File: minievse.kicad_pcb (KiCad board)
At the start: 2 copper layers, 76.2 x 50.8 mm, 27 parts, among them IC1 ATMEGA328P-P, P1 SERIAL, P2 -- 12V ++, P3 ICSP, P4 Pilot, P5 RELAYCOIL, SW1 RESET, U1 7805, U2 IXDD604PI, X1 16MHz

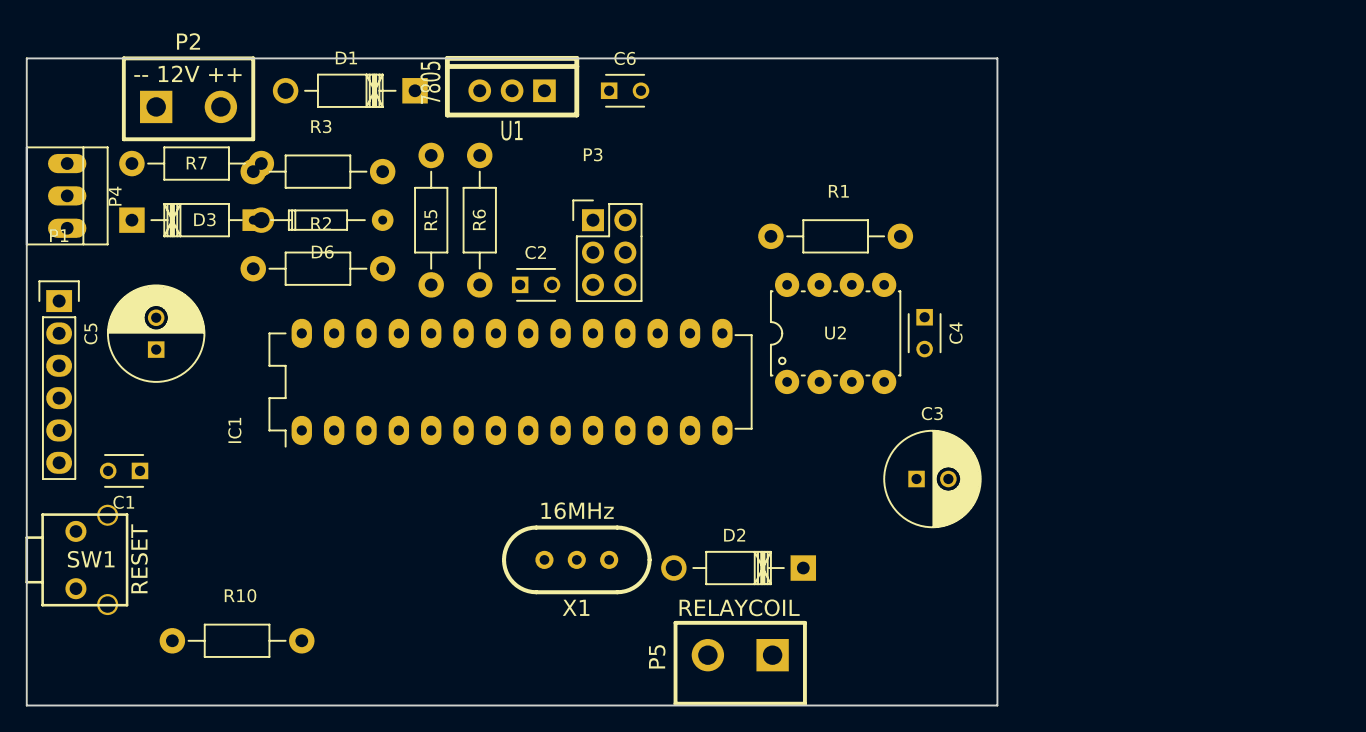
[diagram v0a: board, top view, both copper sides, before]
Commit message: placed parts on the board, ready for traces
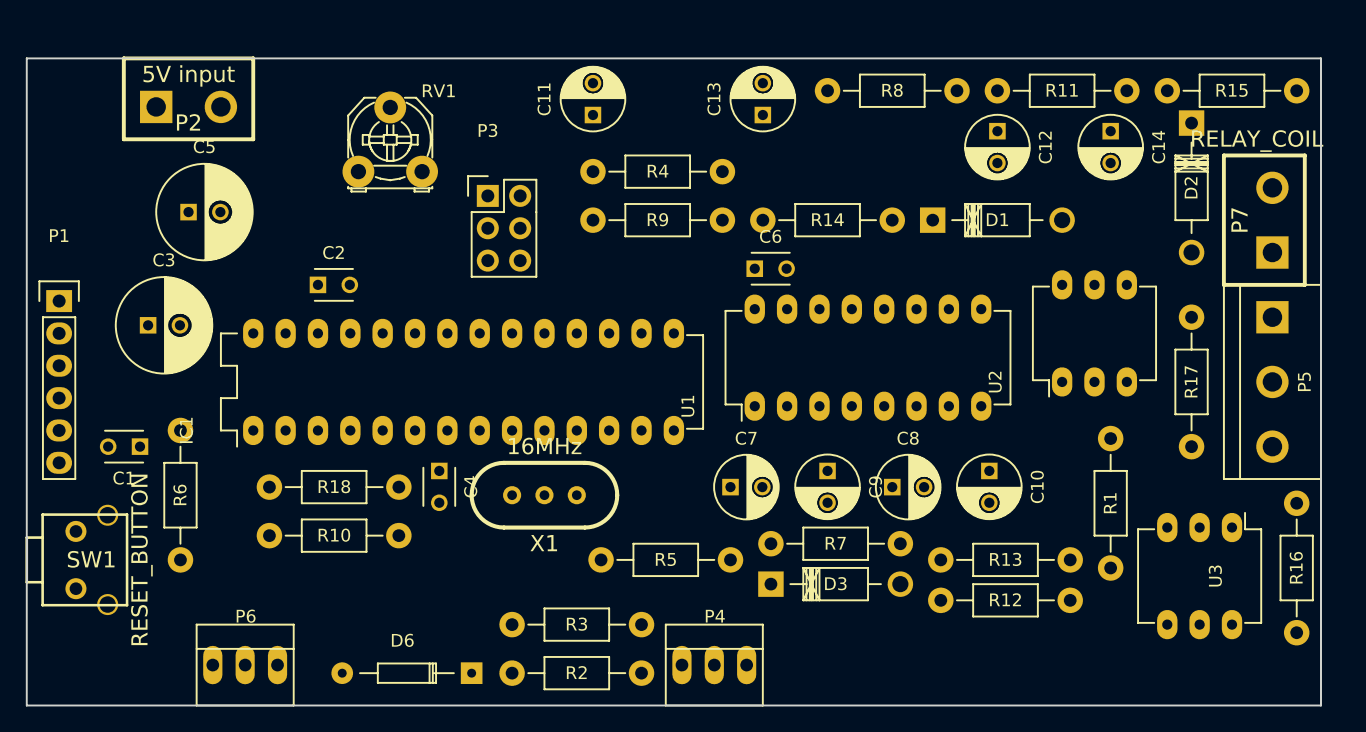
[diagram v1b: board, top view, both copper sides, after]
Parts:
- added C10: 1uF, Capacitors_ThroughHole:C_Radial_D5_L6_P2.5, F.Cu at (101.0, 57.8)
- added C11: 10uF, Capacitors_ThroughHole:C_Radial_D5_L6_P2.5, F.Cu at (69.8, 29.8)
- added C12: 10uF, Capacitors_ThroughHole:C_Radial_D5_L6_P2.5, F.Cu at (101.6, 31.1)
- added C13: 10uF, Capacitors_ThroughHole:C_Radial_D5_L6_P2.5, F.Cu at (83.2, 29.8)
- added C14: 10uF, Capacitors_ThroughHole:C_Radial_D5_L6_P2.5, F.Cu at (110.5, 31.1)
- added C7: 1uF, Capacitors_ThroughHole:C_Radial_D5_L6_P2.5, F.Cu at (80.6, 59.1)
- added C8: 1uF, Capacitors_ThroughHole:C_Radial_D5_L6_P2.5, F.Cu at (93.3, 59.1)
- added C9: 1uF, Capacitors_ThroughHole:C_Radial_D5_L6_P2.5, F.Cu at (88.3, 57.8)
- added P6: LED_STRIP, Connect:PINHEAD1-3, F.Cu at (42.5, 73.0)
- added P7: RELAY_COIL, battery-dlg:CCFLHV, F.Cu at (123.2, 38.1)
- added R11: 2550, wishparts:Resistor_Horizontal_RM10mm_refdes_in_box, F.Cu at (111.8, 27.9)
- added R12: 1200, wishparts:Resistor_Horizontal_RM10mm_refdes_in_box, F.Cu at (97.2, 67.9)
- added R13: 1200, wishparts:Resistor_Horizontal_RM10mm_refdes_in_box, F.Cu at (97.2, 64.8)
- added R14: 50K, wishparts:Resistor_Horizontal_RM10mm_refdes_in_box, F.Cu at (83.2, 38.1)
- added R15: 50K, wishparts:Resistor_Horizontal_RM10mm_refdes_in_box, F.Cu at (114.9, 27.9)
- added R16: 15K, wishparts:Resistor_Horizontal_RM10mm_refdes_in_box, F.Cu at (125.1, 70.5)
- added R17: 15K, wishparts:Resistor_Horizontal_RM10mm_refdes_in_box, F.Cu at (116.8, 55.9)
- added R18: 10K, wishparts:Resistor_Horizontal_RM10mm_refdes_in_box, F.Cu at (44.5, 59.1)
- added R4: 2550, wishparts:Resistor_Horizontal_RM10mm_refdes_in_box, F.Cu at (69.8, 34.3)
- added R8: 2550, wishparts:Resistor_Horizontal_RM10mm_refdes_in_box, F.Cu at (98.4, 27.9)
- added R9: 2550, wishparts:Resistor_Horizontal_RM10mm_refdes_in_box, F.Cu at (80.0, 38.1)
- added RV1: POT, Potentiometers:Potentiometer_Triwood_RM-065, F.Cu at (51.4, 34.3)
- added U3: H11AA, Housings_DIP:DIP-6_W7.62mm_LongPads, F.Cu at (120.0, 62.2)
- D1, D2: footprint Diodes_ThroughHole:Diode_DO-41_SOD81_Horizontal_RM10 -> wishparts:Diode_DO-41_SOD81_Horizontal_RM10_refdes_in_box
- D3: value 13V ZENER -> P6KE16CA; footprint Diodes_ThroughHole:Diode_DO-41_SOD81_Horizontal_RM10 -> wishparts:Diode_DO-41_SOD81_Horizontal_RM10_refdes_in_box
- P2: value -- 12V ++ -> 5V input
- P5: value RELAYCOIL -> AC_GND_AC; footprint battery-dlg:CCFLHV -> Connect:bornier3
- R1: value 650 -> 220; footprint Resistors_ThroughHole:Resistor_Horizontal_RM10mm -> wishparts:Resistor_Horizontal_RM10mm_refdes_in_box
- R10, R2, R3, R5, R6, R7: footprint Resistors_ThroughHole:Resistor_Horizontal_RM10mm -> wishparts:Resistor_Horizontal_RM10mm_refdes_in_box
- SW1: value RESET -> RESET_BUTTON
- U1: value 7805 -> MAX232; footprint battery-dlg:TO220_7805 -> Housings_DIP:DIP-16_W7.62mm_LongPads
- U2: value IXDD604PI -> MOC3021M; footprint Power_Integrations:PDIP-8 -> Housings_DIP:DIP-6_W7.62mm_LongPads
- moved R7 67.3 mm to (94.0, 63.5), turned to 180 degrees
- moved P4 62.7 mm to (79.4, 73.0), turned to 0 degrees
- moved C3 61.5 mm to (34.9, 46.4)
- moved D3 57.7 mm to (83.8, 66.7)
- moved P5 47.0 mm to (123.2, 50.8), turned to 270 degrees
- moved R3 46.8 mm to (73.7, 69.8), turned to 180 degrees
- moved D2 46.4 mm to (116.8, 30.5), turned to 270 degrees
- moved D1 41.9 mm to (96.5, 38.1), turned to 0 degrees
- moved C4 40.0 mm to (57.8, 57.8)
- moved D6 39.5 mm to (60.3, 73.7), turned to 180 degrees
- moved R2 37.7 mm to (63.5, 73.7)
- moved R5 34.4 mm to (70.5, 64.8), turned to 0 degrees
- moved R6 31.9 mm to (37.5, 64.8)
- moved U1 31.2 mm to (82.5, 52.7)
- moved R1 31.0 mm to (110.5, 55.2), turned to 270 degrees
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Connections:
- C3 pad 1: VCC -> +5VD
- C4 pad 1: VCC -> +5VD
- C5 pad 1: VDD -> +5VD
- C6 pad 1: VDD -> +5VD
- D1 pad 1: VCC -> Net-(D1-Pad1)
- D2 pad 1: /RELAY_COIL -> Net-(D2-Pad1)
- D2 pad 2: GND -> Net-(C15-Pad1)
- D3 pad 1: /PILOT -> GND
- D3 pad 2: GND -> /PILOT
- IC1 pad 12: Net-(IC1-Pad12) -> /LED_DATA
- IC1 pad 14: /RELAY -> Net-(IC1-Pad14)
- IC1 pad 15: Net-(IC1-Pad15) -> /RELAY_TRIAC
- IC1 pad 20: VDD -> +5VD
- IC1 pad 23: /AMP_READ -> /AMP_KNOB
- IC1 pad 27: Net-(IC1-Pad27) -> /AC_SENSE_1
- IC1 pad 28: Net-(IC1-Pad28) -> /AC_SENSE_2
- IC1 pad 4: Net-(IC1-Pad4) -> /AC_ZEROX
- IC1 pad 7: VDD -> +5VD
- IC1 pad 8: Net-(IC1-Pad8) -> GND
- P1 pad 3: VDD -> +5VD
- P2 pad 2: Net-(D1-Pad2) -> +5VD
- P3 pad 2: VDD -> +5VD
- P5 pad 1: /RELAY_COIL -> Net-(C15-Pad1)
- R1 pad 1: /PILOT -> Net-(R1-Pad1)
- R1 pad 2: Net-(R1-Pad2) -> /RELAY_TRIAC
- R10 pad 1: VDD -> +5VD
- R3 pad 2: VDD -> +5VD
- R5 pad 1: VDD -> +5VD
- U2 pad 1: Net-(U2-Pad1) -> Net-(R1-Pad1)
- U2 pad 2: /PWM -> GND
- U2 pad 3: GND -> (no net)
- U2 pad 4: /RELAY -> Net-(P7-Pad2)
- U2 pad 5: /RELAY_COIL -> (no net)
- U2 pad 6: VCC -> Net-(D1-Pad2)
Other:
- board size 76.2 x 50.8 mm -> 101.6 x 50.8 mm

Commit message: c10 polarized cap was backwards
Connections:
- C10 pad 1: Net-(C10-Pad1) -> GND
- C10 pad 2: GND -> Net-(C10-Pad2)
- U1 pad 6: Net-(C10-Pad1) -> Net-(C10-Pad2)
- U3 pad 1: Net-(R16-Pad1) -> Net-(R17-Pad1)
- U3 pad 2: Net-(R17-Pad1) -> Net-(R16-Pad1)

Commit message: board half done
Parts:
- moved R6 43.2 mm to (80.6, 63.5), turned to 180 degrees
- moved C5 38.4 mm to (76.2, 33.0)
- moved R9 16.6 mm to (96.5, 36.8)
- moved C13 14.8 mm to (97.8, 32.4), turned to 0 degrees
- moved R4 14.6 mm to (84.5, 33.7)
- moved R5 13.4 mm to (57.1, 63.5)
- moved C11 12.7 mm to (82.5, 29.2), turned to 0 degrees
- moved C2 12.7 mm to (61.0, 43.8), turned to 180 degrees
- moved R14 9.71 mm to (92.7, 40.0)
- moved P3 5.85 mm to (65.4, 31.8)
- moved D1 4.02 mm to (100.3, 36.8)
- moved R1 3.42 mm to (113.7, 54.0), turned to 180 degrees
- moved C12 2.84 mm to (104.1, 32.4), turned to 0 degrees
- moved RV1 2.54 mm to (54.0, 34.3)
- moved C10 1.80 mm to (99.7, 59.1), turned to 0 degrees
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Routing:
- net /AC_SENSE_2: track 0.00 -> 81.6 mm
- net +5VD: track 0.00 -> 65.9 mm
- net /AC_SENSE_1: track 0.00 -> 63.5 mm
- net /reset: track 0.00 -> 38.6 mm, vias 0 -> 3
- net Net-(R13-Pad2): track 0.00 -> 36.8 mm, vias 0 -> 2
- net Net-(D1-Pad2): track 0.00 -> 36.4 mm
- net /PWM: track 0.00 -> 36.2 mm
- net /RELAY_TRIAC: track 0.00 -> 30.7 mm
- net /PILOT: track 0.00 -> 28.0 mm
- net /miso: track 0.00 -> 22.7 mm
- net Net-(R12-Pad2): track 0.00 -> 20.9 mm
- net /AMP_KNOB: track 0.00 -> 17.9 mm
- net /sck: track 0.00 -> 16.6 mm, vias 0 -> 1
- net Net-(C15-Pad1): track 0.00 -> 16.5 mm
- net Net-(P7-Pad2): track 0.00 -> 15.8 mm
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
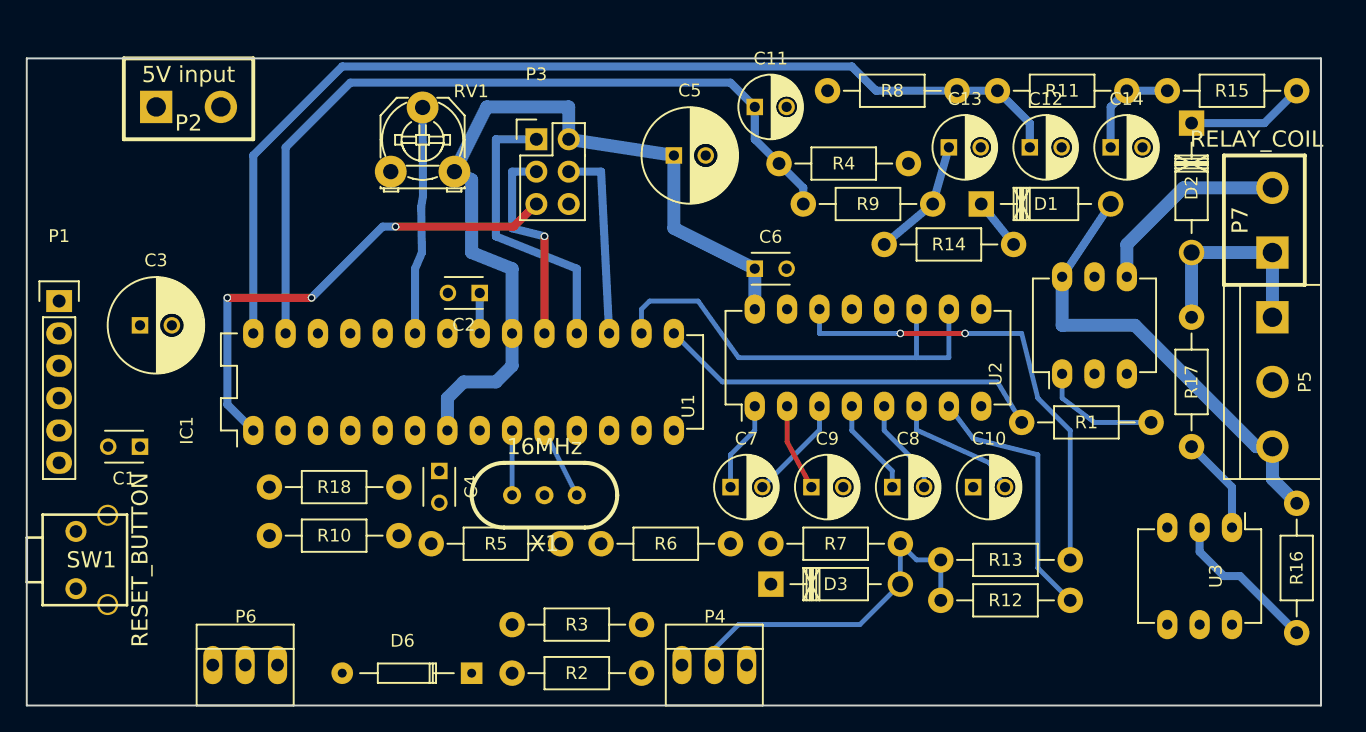
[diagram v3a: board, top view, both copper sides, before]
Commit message: move things around for mounting holes in corners
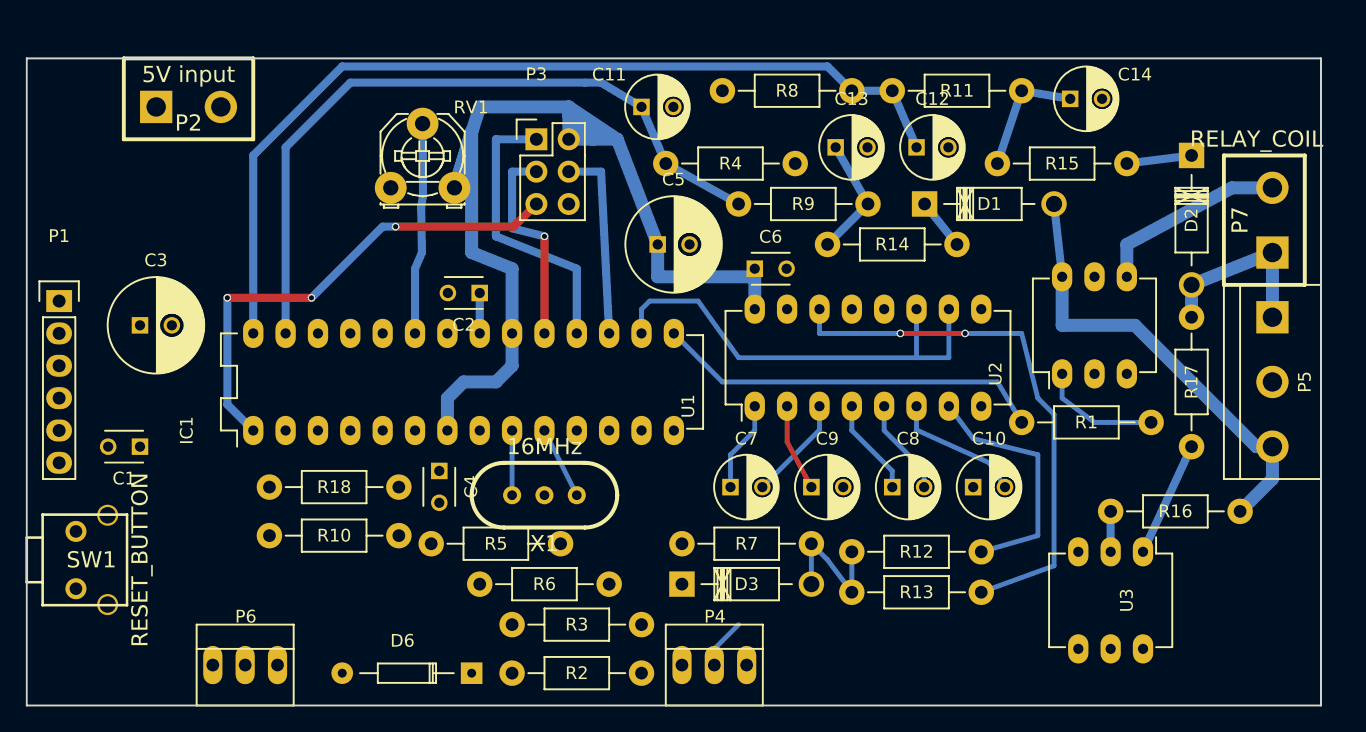
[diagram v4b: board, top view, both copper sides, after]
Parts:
- moved R16 17.4 mm to (110.5, 61.0), turned to 0 degrees
- moved R15 14.5 mm to (101.6, 33.7)
- moved R6 10.0 mm to (71.1, 66.7)
- moved C11 8.89 mm to (73.7, 29.2)
- moved C12 8.89 mm to (95.2, 32.4)
- moved C13 8.89 mm to (88.9, 32.4)
- moved R4 8.89 mm to (75.6, 33.7)
- moved R11 8.26 mm to (103.5, 27.9)
- moved R8 8.25 mm to (90.2, 27.9)
- moved R12 7.96 mm to (90.2, 64.1)
- moved R13 7.43 mm to (90.2, 67.3)
- moved U3 7.24 mm to (113.0, 64.1)
- moved C5 7.10 mm to (74.9, 40.0)
- moved D3 6.98 mm to (76.8, 66.7)
- moved R7 6.98 mm to (87.0, 63.5)
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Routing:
- net +5VD: track 65.9 -> 82.7 mm
- net /PILOT: track 28.0 -> 15.3 mm
- net Net-(R16-Pad1): track 12.2 -> 3.18 mm
- net /AC_SENSE_2: track 81.6 -> 72.7 mm
- net /AC_SENSE_1: track 63.5 -> 56.6 mm
- net Net-(R13-Pad2): track 36.8 -> 42.8 mm
- net Net-(D2-Pad1): track 9.30 -> 5.12 mm
- net Net-(C15-Pad1): track 16.5 -> 14.5 mm
- net Net-(C14-Pad1): track 8.15 -> 9.89 mm
- net Net-(R12-Pad2): track 20.9 -> 19.4 mm
- net Net-(R17-Pad1): track 7.67 -> 9.09 mm
- net /AMP_KNOB: track 17.9 -> 16.6 mm
- net Net-(P7-Pad2): track 15.8 -> 15.1 mm

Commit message: add mounting holes, run more traces
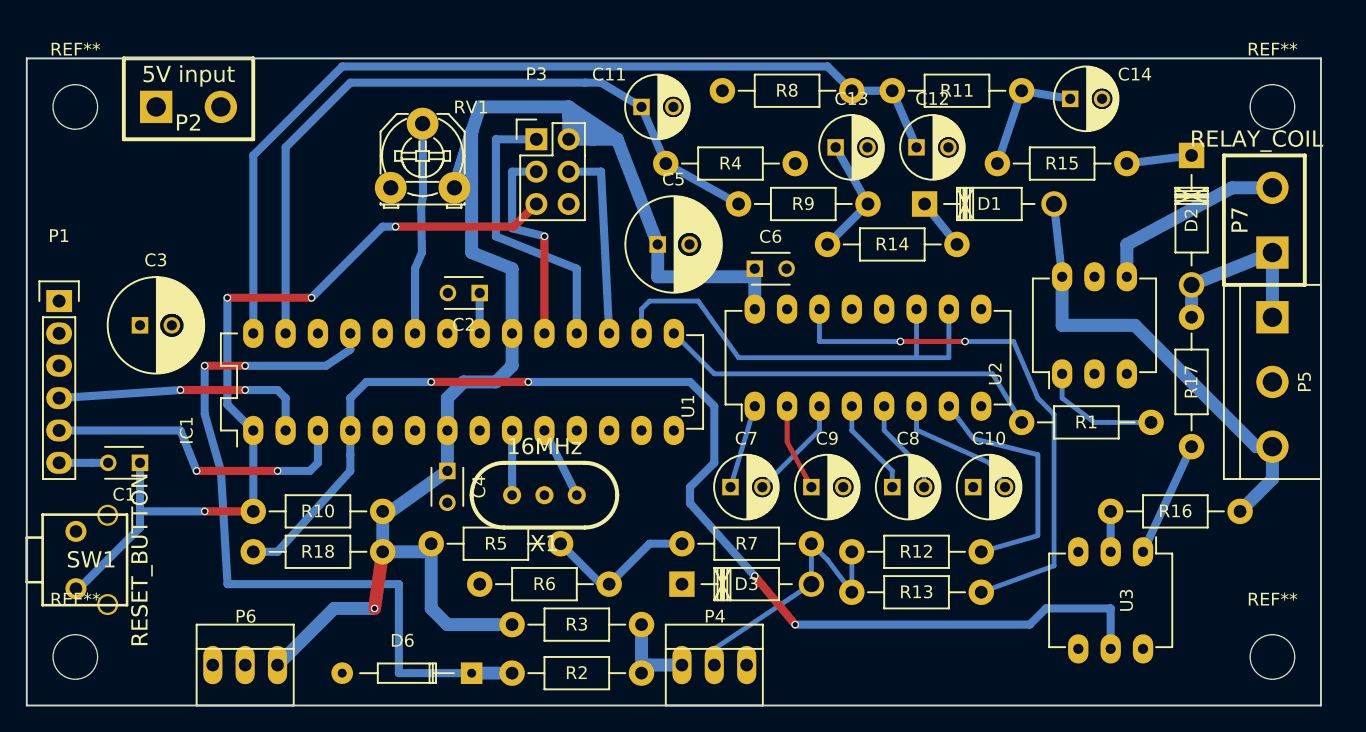
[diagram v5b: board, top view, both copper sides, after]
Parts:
- added REF**: MountingHole_3.5mm, Mounting_Holes:MountingHole_3.5mm, F.Cu at (123.2, 29.2)
- added REF**: MountingHole_3.5mm, Mounting_Holes:MountingHole_3.5mm, F.Cu at (123.2, 72.4)
- added REF**: MountingHole_3.5mm, Mounting_Holes:MountingHole_3.5mm, F.Cu at (29.2, 29.2)
- added REF**: MountingHole_3.5mm, Mounting_Holes:MountingHole_3.5mm, F.Cu at (29.2, 72.4)
- moved R18 10.2 mm to (53.3, 64.1), turned to 180 degrees
- moved R10 9.09 mm to (53.3, 61.0), turned to 180 degrees
- moved C1 1.27 mm to (34.3, 57.1)
- moved C4 0.64 mm to (58.4, 57.8)
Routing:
- net /AC_ZEROX: track 0.00 -> 95.5 mm, vias 0 -> 4
- net /PP_READ: track 0.00 -> 59.7 mm, vias 0 -> 2
- net +5VD: track 82.7 -> 124.5 mm, vias 0 -> 1
- net /reset: track 38.6 -> 65.9 mm, vias 3 -> 4
- net /TX: track 0.00 -> 25.3 mm, vias 0 -> 2
- net /RX: track 0.00 -> 20.6 mm, vias 0 -> 2
- net /PILOTREAD: track 0.00 -> 12.2 mm
- net /PP: track 0.00 -> 7.25 mm
- net /PILOT: track 15.3 -> 21.7 mm
- net Net-(C1-Pad2): track 0.00 -> 3.85 mm
- net Net-(C7-Pad1): track 7.14 -> 6.63 mm
